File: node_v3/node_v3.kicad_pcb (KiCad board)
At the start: 4 copper layers, 76.2 x 45.7 mm, 65 parts, among them J1 Conn_Coaxial, J10 3V3OUT, J12 12402012E212A, J13 DBG, J14 VIN, J15 Conn_01x16_Pin, J2 Micro_SD_Card, J6 BAT, Q1 2N3904, SW1 PTS526, SW2 PTS526, U1 RFM69HCW, U2 MCP7940N-xSN, U3 MCP73831-2-OT, U4 ADP2108AUJ-3.3, U5 CAT3200-5, U6 RP2040, U7 W25Q128JVS, Y1 445C35A12M00000, Y2 SC32S-7PF20PPM

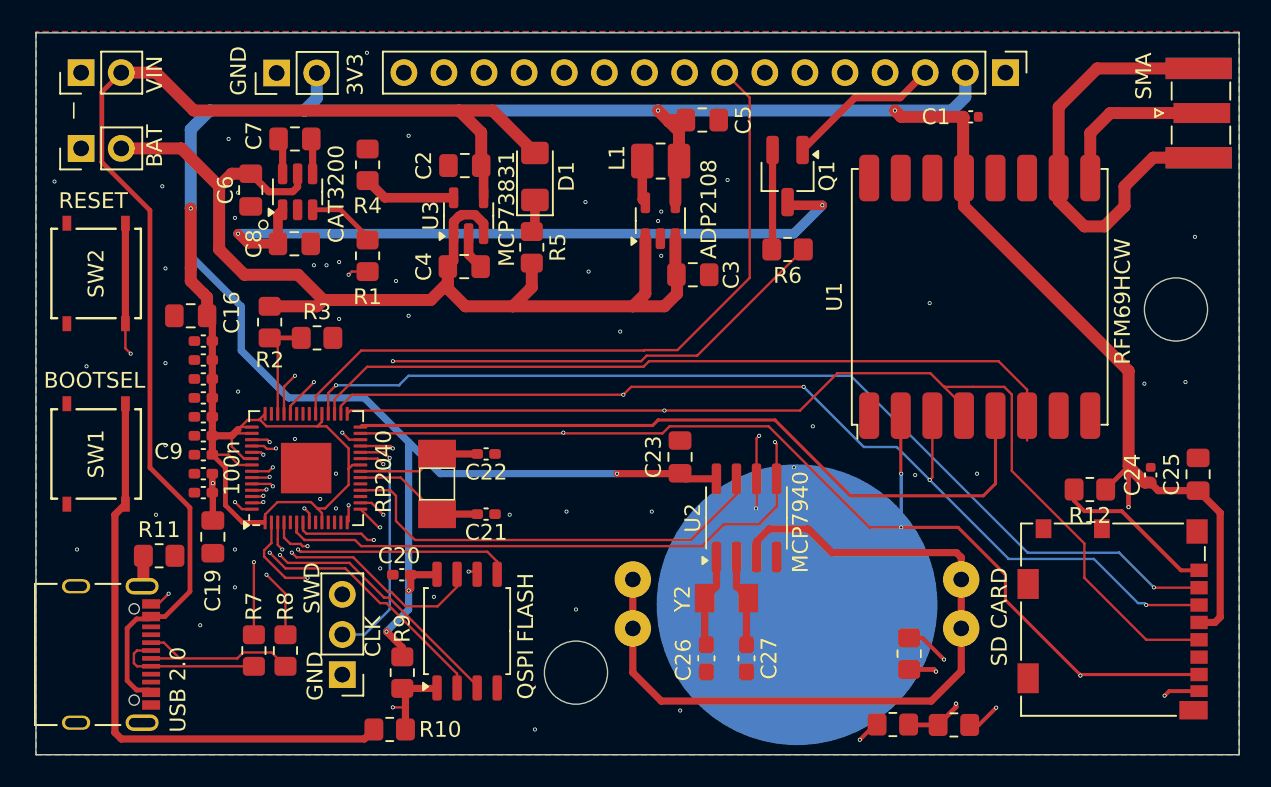
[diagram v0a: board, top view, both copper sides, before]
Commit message: finalized pcb v3, added silkscreen and all and fixed some issues found in the drc
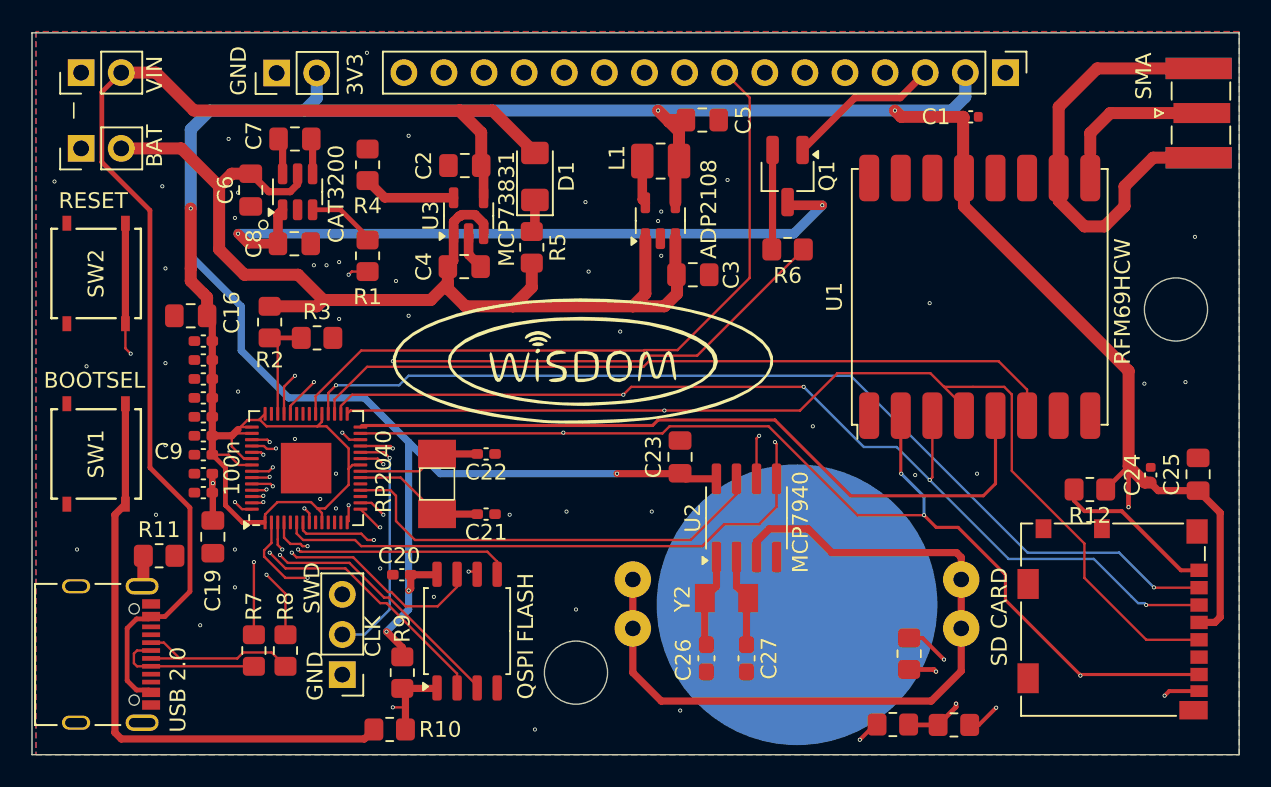
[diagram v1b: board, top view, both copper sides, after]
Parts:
- added G***: LOGO, custom:wisdom_logo_lineborder, F.Cu at (95.2, 68.3)
- added LOGO: , custom:qrcode, B.Cu at (128.8, 84.3)
- added LOGO: , custom:github_qr, B.Cu at (116.3, 63.0)
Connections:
- BT1 pad 2: GND -> Net-(BT1-+)
- BT1 pad 3: (no net) -> Net-(BT1-+)
- BT1 pad 4: (no net) -> Net-(BT1-+)
- BT1 pad 5: (no net) -> GND
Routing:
- net MISO: track 103.8 -> 100.1 mm
- net I2C_SCK: track 59.2 -> 62.2 mm, vias 3 -> 2
- net RFM_RST: track 49.7 -> 48.2 mm
- net GND: track 31.7 -> 30.8 mm, vias 49 -> 47
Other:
- board size 76.2 x 45.7 mm -> 76.5 x 45.7 mm
- board text added: "WiSDOM Github"
- board text added: "WiSDOM Node v3 March 2024 By Amelia Vlahogiannis"
- board text added: "wisdomresearch.net"
- board text removed: "WiSDOM Node v3.0 March 2024 By Amelia Vlahogiannis"
